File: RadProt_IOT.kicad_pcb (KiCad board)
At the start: 2 copper layers, 10 parts, among them J1 Conn_01x04_Pin, J2 Conn_01x04_Pin, J3 Conn_01x04_Pin, J4 OUT+, J5 OUT-, J6 Conn_02x05_Top_Bottom, SW1 Config

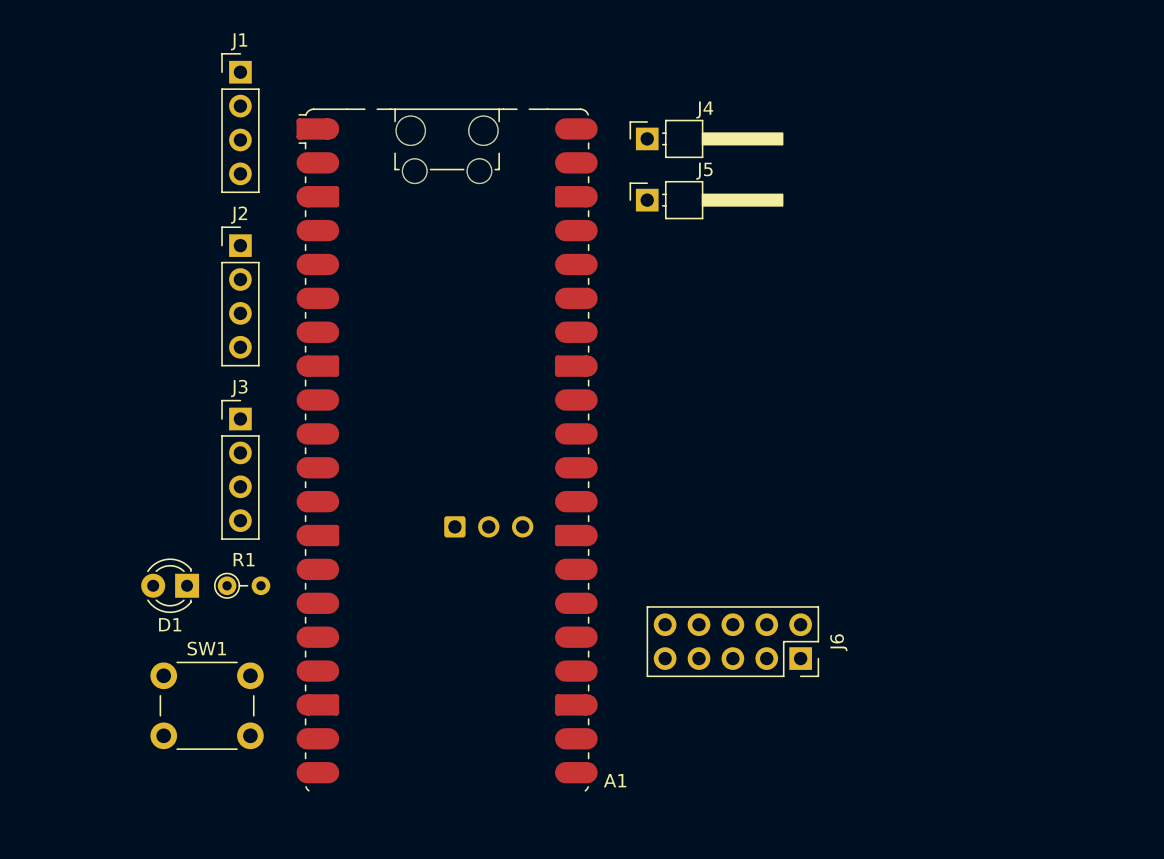
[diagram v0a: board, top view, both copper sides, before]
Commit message: manually routed, 1 route needs bridge
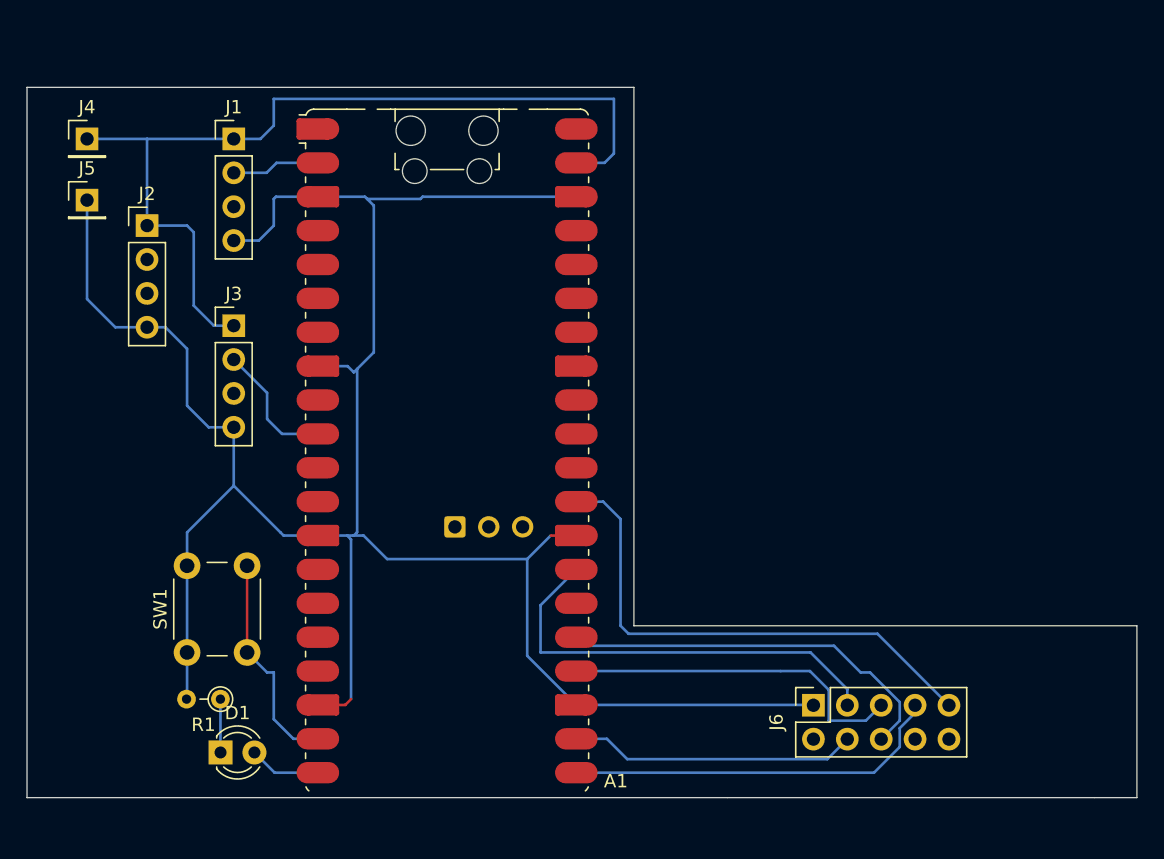
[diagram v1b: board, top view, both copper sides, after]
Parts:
- J4, J5: footprint Connector_PinHeader_2.54mm:PinHeader_1x01_P2.54mm_Horizontal -> Connector_PinHeader_2.54mm:PinHeader_1x01_P2.54mm_Vertical
- moved J4 42.0 mm to (107.5, 84.5)
- moved J5 42.0 mm to (107.5, 89.1)
- moved D1 12.7 mm to (117.5, 130.5), turned to 0 degrees
- moved R1 8.51 mm to (117.5, 126.5), turned to 180 degrees
- moved J2 7.16 mm to (112.0, 91.0)
- moved J3 7.02 mm to (118.5, 98.5)
- moved J1 5.02 mm to (118.5, 84.5)
- moved J6 3.63 mm to (162.0, 127.0), turned to 90 degrees
- moved SW1 2.47 mm to (115.0, 123.0), turned to 90 degrees
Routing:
- net GND: track 0.00 -> 178.4 mm
- net +5V: track 0.00 -> 68.4 mm
- net Net-(A1-GPIO22): track 0.00 -> 39.4 mm
- net Net-(A1-GPIO21): track 0.00 -> 32.7 mm
- net Net-(A1-GPIO19): track 0.00 -> 29.6 mm
- net Net-(A1-GPIO16): track 0.00 -> 28.6 mm
- net Net-(A1-GPIO18): track 0.00 -> 26.2 mm
- net Net-(A1-GPIO17): track 0.00 -> 21.6 mm
- net Net-(A1-GPIO14): track 0.00 -> 16.5 mm
- net /UART3_RX: track 0.00 -> 9.76 mm
- net /UART0_RX: track 0.00 -> 6.61 mm
- net Net-(A1-GPIO15): track 0.00 -> 5.38 mm
- net Net-(D1-K): track 0.00 -> 4.00 mm
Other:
- board outline added: 83.2 x 53.2 mm

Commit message: routed with 1mm
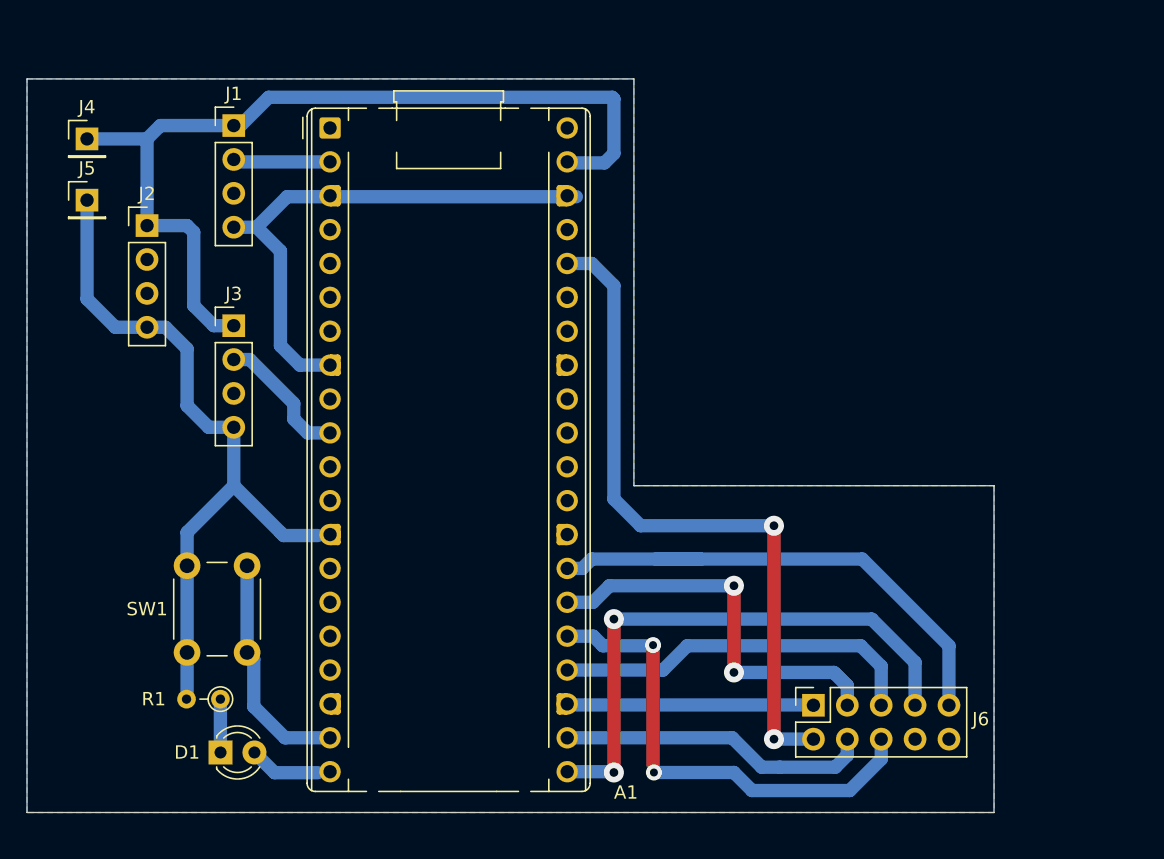
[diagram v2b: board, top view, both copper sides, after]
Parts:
- A1: footprint Module:RaspberryPi_Pico_W_SMD_HandSolder -> Module:RaspberryPi_Pico_Common_THT
- moved A1 25.7 mm to (125.7, 83.7)
- moved J1 1.00 mm to (118.5, 83.5)
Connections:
- A1 pad 26: unconnected-(A1-GPIO20-Pad26) -> Net-(A1-GPIO20)
- A1 pad 29: Net-(A1-GPIO22) -> unconnected-(A1-GPIO22-Pad29)
- J6 pad INT: Net-(A1-GPIO22) -> Net-(A1-GPIO21)
- J6 pad RESET: Net-(A1-GPIO21) -> Net-(A1-GPIO20)
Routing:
- net GND: track 178.4 -> 112.9 mm
- net Net-(A1-3V3): track 0.00 -> 51.5 mm, vias 0 -> 2
- net Net-(A1-GPIO22): track 39.4 -> 0.00 mm
- net Net-(A1-GPIO20): track 0.00 -> 30.6 mm, vias 0 -> 2
- net Net-(A1-GPIO16): track 28.6 -> 41.3 mm, vias 0 -> 2
- net Net-(A1-GPIO21): track 32.7 -> 39.4 mm
- net Net-(A1-GPIO19): track 29.6 -> 35.9 mm, vias 0 -> 2
- net Net-(A1-GPIO17): track 21.6 -> 23.5 mm
- net Net-(A1-GPIO18): track 26.2 -> 27.9 mm
- net +5V: track 68.4 -> 67.4 mm
- net Net-(A1-GPIO14): track 16.5 -> 17.5 mm
- net /UART0_RX: track 6.61 -> 7.29 mm
- added copper zone on B.Cu, net GND
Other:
- board size 83.2 x 53.2 mm -> 72.5 x 55 mm

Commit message: nicer
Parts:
- A1: footprint Module:RaspberryPi_Pico_Common_THT -> Module:RaspberryPi_Pico_W_SMD_HandSolder
- R1: footprint Resistor_THT:R_Axial_DIN0204_L3.6mm_D1.6mm_P2.54mm_Vertical -> Resistor_THT:R_Axial_DIN0204_L3.6mm_D1.6mm_P5.08mm_Horizontal
- moved A1 25.2 mm to (133.6, 107.6)
- moved D1 7.99 mm to (111.5, 125.2), turned to -90 degrees
- moved J1 6.50 mm to (112.0, 83.5)
- moved J2 6.50 mm to (118.5, 91.0)
- moved J3 6.50 mm to (112.0, 98.5)
- moved R1 4.53 mm to (117.0, 131.0)
- moved SW1 3.72 mm to (111.5, 121.8)
- moved J6 3.38 mm to (165.3, 127.0)
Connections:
- D1 pad 1: Net-(D1-K) -> GND
- D1 pad 2: Net-(A1-GPIO15) -> Net-(D1-A)
- R1 pad 1: Net-(D1-K) -> Net-(A1-GPIO15)
- R1 pad 2: GND -> Net-(D1-A)
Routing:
- net Net-(A1-GPIO17): track 23.5 -> 30.3 mm
- net /UART2_RX: track 0.00 -> 5.47 mm
- net +5V: track 67.4 -> 72.6 mm
- net /UART0_RX: track 7.29 -> 11.9 mm
- net Net-(A1-3V3): track 51.5 -> 55.9 mm
- net Net-(A1-GPIO19): track 35.9 -> 40.1 mm
- net Net-(A1-GPIO16): track 41.3 -> 45.4 mm
- net Net-(D1-K): track 4.00 -> 0.00 mm
- net /UART3_RX: track 10.2 -> 14.1 mm
- net Net-(A1-GPIO18): track 27.9 -> 31.5 mm
- net Net-(A1-GPIO20): track 30.6 -> 34.2 mm
- net Net-(D1-A): track 0.00 -> 3.44 mm
- net Net-(A1-GPIO21): track 39.4 -> 42.1 mm
- net Net-(A1-GPIO14): track 17.5 -> 19.7 mm
- net Net-(A1-GPIO15): track 5.38 -> 7.23 mm
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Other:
- board size 72.5 x 55 mm -> 76 x 55 mm
- board text added: "dfas"

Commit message: nicer +10
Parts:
- D1: value STATUS -> Status
- moved J4 7.91 mm to (107.5, 92.4)
- moved J5 7.91 mm to (107.5, 97.0)
- moved J1 1.50 mm to (112.0, 82.0)
- moved J3 1.50 mm to (112.0, 100.0)
- moved J6 1.50 mm to (166.8, 127.0)
- moved J2 0.50 mm to (118.0, 91.0)
- renumbered A1 to U1
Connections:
- J1 pad 3: unconnected-(J1-Pin_3-Pad3) -> (no net)
- J2 pad 3: unconnected-(J2-Pin_3-Pad3) -> (no net)
- J3 pad 3: unconnected-(J3-Pin_3-Pad3) -> (no net)
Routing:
- net +5V: track 72.6 -> 80.1 mm
- net GND: track 114.7 -> 108.0 mm
- net Net-(U1-GPIO21): track 42.1 -> 43.6 mm
- net Net-(U1-GPIO20): track 34.2 -> 35.7 mm
- net Net-(U1-GPIO18): track 31.5 -> 33.0 mm
- net Net-(U1-GPIO17): track 30.3 -> 31.8 mm
- net Net-(U1-GPIO16): track 45.4 -> 46.9 mm
- net Net-(U1-GPIO19): track 40.1 -> 41.6 mm
- net Net-(U1-3V3): track 55.9 -> 56.6 mm
- net /UART3_RX: track 14.1 -> 13.5 mm
- net /UART0_RX: track 11.9 -> 12.5 mm
- net /UART2_RX: track 5.47 -> 5.97 mm
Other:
- outline, holes or cut-outs redrawn
- board text added: "+5V"
- board text added: "GND"
- board text added: "RX"
- board text added: "TX"
- board text removed: "dfas"

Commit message: nice +30
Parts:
- renumbered J4 to +5v, J5 to GND
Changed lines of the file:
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@@
 		(descr "Through hole straight pin header, 1x01, 2.54mm pitch, single row")
 		(tags "Through hole pin header THT 1x01 2.54mm single row")
-		(property "Reference" "J4"
+		(property "Reference" "+5v"
 			(at 2.5 -0.01 0)
 			(layer "F.SilkS")
@@
 		(descr "Through hole straight pin header, 1x01, 2.54mm pitch, single row")
 		(tags "Through hole pin header THT 1x01 2.54mm single row")
-		(property "Reference" "J5"
+		(property "Reference" "GND"
 			(at 2.9 0 0)
 			(layer "F.SilkS")
